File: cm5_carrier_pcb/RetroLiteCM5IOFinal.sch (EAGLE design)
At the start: 325 parts, among them J1 5025700893, J10 5051100892, J11 1072TR, J12 5034802000, J13 5040500491, J14 5051100492, J2 SJ-43516-SMT, J4 5051100492, J5 685119136923, J6 5034802000, J7 105450-0101, J8 MDT320E01001, J9 5051103091, Q1 AO3400A, Q2 AO3400A, Q3 AO3400A, Q4 AO3400A, Q5 AO3400A, Q6 AO3400A, Q7 AO3400A, Q8 AO3400A, Q9 AO3400A, U10 UM3204QQFN14_3.5X3.5_UM3204_U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, U11 MAX17055ETB+T, U12 SY8089AAACSY8089AAAC_SGY-L, U13 UM3204QQFN14_3.5X3.5_UM3204_U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, U14 MCU-ATTINY84A-MU(QFN20), U16 TPS61160ADRVT, U18 TSIC_306_SOP-8, U2 TPD4E05U06DQAR, U21 TPS65987DDHRSHR, U22 TPD4E05U06DQAR, U23 TUSB546-DCIRNQT, U24 TPD4E05U06DQAR, U3 TPD4E05U06DQAR, U4 W25X05CLUXIGTR, U5 BQ24292I, U6 WM8960, U7 TPS61235PRWLT, U8 UM3204QQFN14_3.5X3.5_UM3204_U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, U9 UM3204QQFN14_3.5X3.5_UM3204_U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, Y1 ECS-3225MV-240-BN-TR, Y2 ECS-.327-12.5-12R-TR

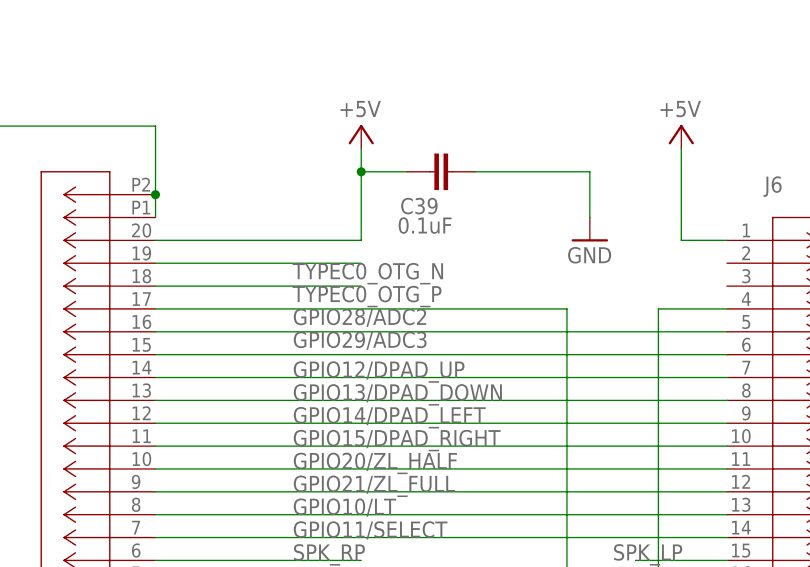
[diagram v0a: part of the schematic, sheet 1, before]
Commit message: Swap back OTG/host lanes
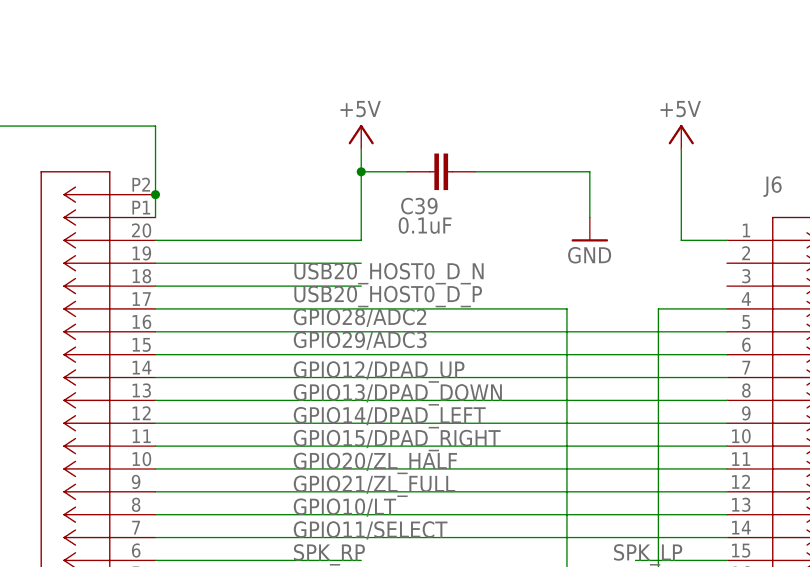
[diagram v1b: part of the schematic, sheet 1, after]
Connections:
- net GPIO0_C2: now also GPIO1_B1_V-.TP; no longer GPIO0_C2_V+.TP
- net GPIO1_B1: now also GPIO0_C2_V+.TP; no longer GPIO1_B1_V-.TP
- net TYPEC0_OTG_N: now also J7.D1-, J7.D2-; no longer J12.19
- net TYPEC0_OTG_P: now also J7.D1+, J7.D2+; no longer J12.18
- net USB20_HOST0_D_N: now also J12.19; no longer J7.D1-, J7.D2-
- net USB20_HOST0_D_P: now also J12.18; no longer J7.D1+, J7.D2+
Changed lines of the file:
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@@
 <part name="NEXTRST" library="testpad" deviceset="TP" device="TP07R"/>
 <part name="GPIO14_HPD" library="testpad" deviceset="TP" device="TP07R"/>
-<part name="GPIO1_B1_V-" library="testpad" deviceset="TP" device="TP07R"/>
+<part name="GPIO0_C2_V+" library="testpad" deviceset="TP" device="TP07R"/>
 <part name="U21" library="TPS65987DDHRSHR" deviceset="TPS65987DDHRSHR" device=""/>
 <part name="U23" library="TUSB546-DCIRNQT" deviceset="TUSB546-DCIRNQT" device=""/>
@@
 <part name="P+17" library="supply1" deviceset="VCC" device=""/>
 <part name="GND108" library="supply1" deviceset="GND" device=""/>
-<part name="GPIO0_C2_V+" library="testpad" deviceset="TP" device="TP07R"/>
+<part name="GPIO1_B1_V-" library="testpad" deviceset="TP" device="TP07R"/>
 <part name="C9" library="rcl" deviceset="C-EU" device="C0402-YVELTAL" package3d_urn="urn:adsk.eagle:package:2745540/2" value="100nF"/>
 <part name="C78" library="resistor" library_urn="urn:adsk.eagle:library:348" deviceset="C-EU" device="C0603" package3d_urn="urn:adsk.eagle:package:23616/2" value="10uF"/>
@@
 <attribute name="TP_SIGNAL_NAME" x="427.99" y="293.37" size="1.778" layer="97" rot="R90"/>
 </instance>
-<instance part="GPIO1_B1_V-" gate="G$1" x="426.72" y="297.18" smashed="yes" rot="R90">
+<instance part="GPIO0_C2_V+" gate="G$1" x="426.72" y="297.18" smashed="yes" rot="R90">
 <attribute name="TP_SIGNAL_NAME" x="427.99" y="298.45" size="1.778" layer="97" rot="R90"/>
 </instance>
@@
 <attribute name="VALUE" x="825.5" y="205.74" size="1.778" layer="96" font="vector"/>
 </instance>
-<instance part="GPIO0_C2_V+" gate="G$1" x="426.72" y="281.94" smashed="yes" rot="R90">
+<instance part="GPIO1_B1_V-" gate="G$1" x="426.72" y="281.94" smashed="yes" rot="R90">
 <attribute name="TP_SIGNAL_NAME" x="427.99" y="283.21" size="1.778" layer="97" rot="R90"/>
 </instance>
@@
 </segment>
 <segment>
-<pinref part="GPIO0_C2_V+" gate="G$1" pin="TP"/>
+<pinref part="GPIO1_B1_V-" gate="G$1" pin="TP"/>
 <label x="431.8" y="281.94" size="1.778" layer="95" font="vector"/>
 <wire x1="429.26" y1="281.94" x2="439.42" y2="281.94" width="0.1524" layer="91"/>
@@
 <pinref part="CONNECTOR3" gate="G$1" pin="35"/>
 </segment>
+<segment>
+<wire x1="728.98" y1="144.78" x2="751.84" y2="144.78" width="0.1524" layer="91"/>
+<label x="744.22" y="144.78" size="1.778" layer="95" font="vector" rot="MR180"/>
+<pinref part="J12" gate="A" pin="19"/>
+</segment>
 </net>
 <net name="USB20_HOST0_D_P" class="13">
@@
 <pinref part="CONNECTOR3" gate="G$1" pin="37"/>
 </segment>
+<segment>
+<wire x1="728.98" y1="142.24" x2="751.84" y2="142.24" width="0.1524" layer="91"/>
+<label x="744.22" y="142.24" size="1.778" layer="95" font="vector" rot="MR180"/>
+<pinref part="J12" gate="A" pin="18"/>
+</segment>
 </net>
 <net name="CM5_3.3V(OUTPUT)" class="0">
@@
 <wire x1="271.78" y1="525.78" x2="246.38" y2="525.78" width="0.1524" layer="91"/>
 </segment>
-<segment>
-<wire x1="728.98" y1="144.78" x2="751.84" y2="144.78" width="0.1524" layer="91"/>
-<label x="744.22" y="144.78" size="1.778" layer="95" font="vector" rot="MR180"/>
-<pinref part="J12" gate="A" pin="19"/>
-</segment>
 </net>
 <net name="TYPEC0_OTG_P" class="1">
@@
 <label x="243.84" y="523.24" size="1.778" layer="95" font="vector" rot="R180"/>
 </segment>
-<segment>
-<wire x1="728.98" y1="142.24" x2="751.84" y2="142.24" width="0.1524" layer="91"/>
-<label x="744.22" y="142.24" size="1.778" layer="95" font="vector" rot="MR180"/>
-<pinref part="J12" gate="A" pin="18"/>
-</segment>
 </net>
 <net name="PCIE20X1_2_PERSTN_M0" class="0">
@@
 <net name="GPIO1_B1" class="0">
 <segment>
-<pinref part="GPIO1_B1_V-" gate="G$1" pin="TP"/>
+<pinref part="GPIO0_C2_V+" gate="G$1" pin="TP"/>
 <label x="431.8" y="297.18" size="1.778" layer="95" font="vector"/>
 <wire x1="429.26" y1="297.18" x2="439.42" y2="297.18" width="0.1524" layer="91"/>
@@
 </segment>
 </net>
-<net name="USB20_HOST0_D_N" class="13">
-<segment>
-<pinref part="J7" gate="G$1" pin="D2-"/>
-<wire x1="139.7" y1="535.94" x2="147.32" y2="535.94" width="0.1524" layer="91"/>
-<wire x1="147.32" y1="535.94" x2="147.32" y2="541.02" width="0.1524" layer="91"/>
-<pinref part="J7" gate="G$1" pin="D1-"/>
-<wire x1="147.32" y1="541.02" x2="139.7" y2="541.02" width="0.1524" layer="91"/>
-<label x="147.32" y="535.94" size="1.778" layer="95" font="vector"/>
-<wire x1="147.32" y1="535.94" x2="154.94" y2="535.94" width="0.1524" layer="91"/>
-<junction x="147.32" y="535.94"/>
-</segment>
-</net>
-<net name="USB20_HOST0_D_P" class="13">
-<segment>
-<pinref part="J7" gate="G$1" pin="D1+"/>
-<wire x1="139.7" y1="543.56" x2="144.78" y2="543.56" width="0.1524" layer="91"/>
-<wire x1="144.78" y1="543.56" x2="144.78" y2="538.48" width="0.1524" layer="91"/>
-<pinref part="J7" gate="G$1" pin="D2+"/>
-<wire x1="144.78" y1="538.48" x2="139.7" y2="538.48" width="0.1524" layer="91"/>
-<label x="147.32" y="543.56" size="1.778" layer="95" font="vector"/>
-<wire x1="144.78" y1="543.56" x2="154.94" y2="543.56" width="0.1524" layer="91"/>
-<junction x="144.78" y="543.56"/>
-</segment>
-</net>
 <net name="EINT_CTP1" class="0">
 <segment>
@@
 </segment>
 </net>
+<net name="TYPEC0_OTG_N" class="1">
+<segment>
+<pinref part="J7" gate="G$1" pin="D2-"/>
+<wire x1="139.7" y1="535.94" x2="147.32" y2="535.94" width="0.1524" layer="91"/>
+<wire x1="147.32" y1="535.94" x2="147.32" y2="541.02" width="0.1524" layer="91"/>
+<pinref part="J7" gate="G$1" pin="D1-"/>
+<wire x1="147.32" y1="541.02" x2="139.7" y2="541.02" width="0.1524" layer="91"/>
+<label x="147.32" y="535.94" size="1.778" layer="95" font="vector"/>
+<wire x1="147.32" y1="535.94" x2="154.94" y2="535.94" width="0.1524" layer="91"/>
+<junction x="147.32" y="535.94"/>
+</segment>
+</net>
+<net name="TYPEC0_OTG_P" class="1">
+<segment>
+<pinref part="J7" gate="G$1" pin="D1+"/>
+<wire x1="139.7" y1="543.56" x2="144.78" y2="543.56" width="0.1524" layer="91"/>
+<wire x1="144.78" y1="543.56" x2="144.78" y2="538.48" width="0.1524" layer="91"/>
+<pinref part="J7" gate="G$1" pin="D2+"/>
+<wire x1="144.78" y1="538.48" x2="139.7" y2="538.48" width="0.1524" layer="91"/>
+<label x="147.32" y="543.56" size="1.778" layer="95" font="vector"/>
+<wire x1="144.78" y1="543.56" x2="154.94" y2="543.56" width="0.1524" layer="91"/>
+<junction x="144.78" y="543.56"/>
+</segment>
+</net>
